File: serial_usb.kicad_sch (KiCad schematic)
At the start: 24 parts, among them J2 3V3 Serial, J3 USB_C_USB2.0_16P, U17 ST16C550, U18 CP2102N, Y2 7.3728MHz

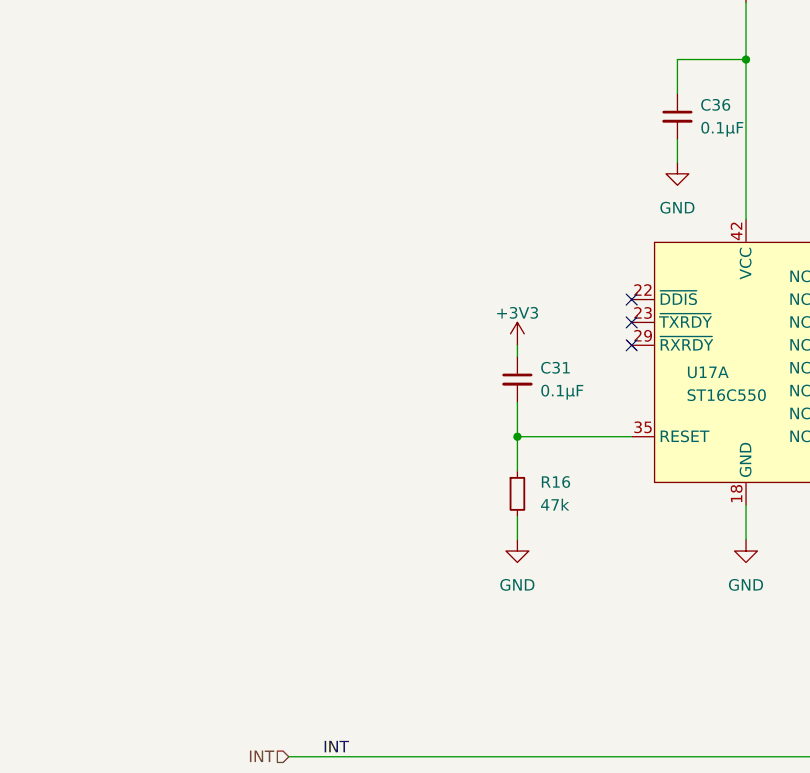
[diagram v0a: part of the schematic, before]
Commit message: Rework RESET/RST: see Changelist
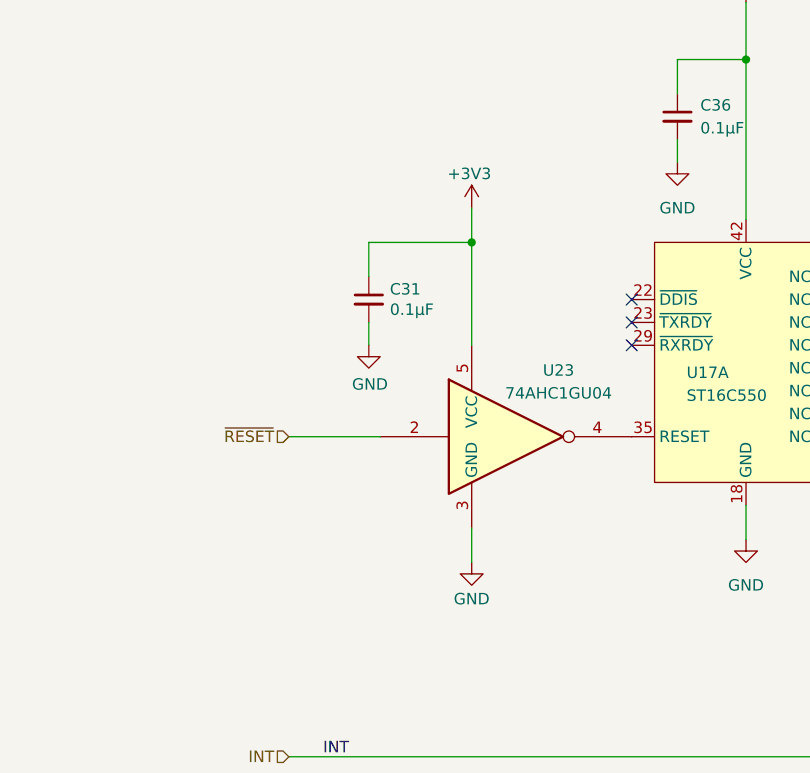
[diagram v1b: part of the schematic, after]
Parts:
- removed R16: 47k, Resistor_SMD:R_0402_1005Metric, symbol Device:R_Small
- added U23: 74AHC1GU04, Package_TO_SOT_SMD:SOT-23-5, symbol 74xGxx:74AHC1GU04
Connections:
- net +3V3: now also U23.5 (VCC)
- net GND: now also C31.2, U23.3 (GND)
- net at U17.35 (RESET): now also U23.4; no longer C31.2
- new net ~{RESET}: U23.2
